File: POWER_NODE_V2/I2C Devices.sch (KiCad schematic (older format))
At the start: 20 parts

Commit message: more WIP
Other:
- moved on the sheet: Q?, R?, U?

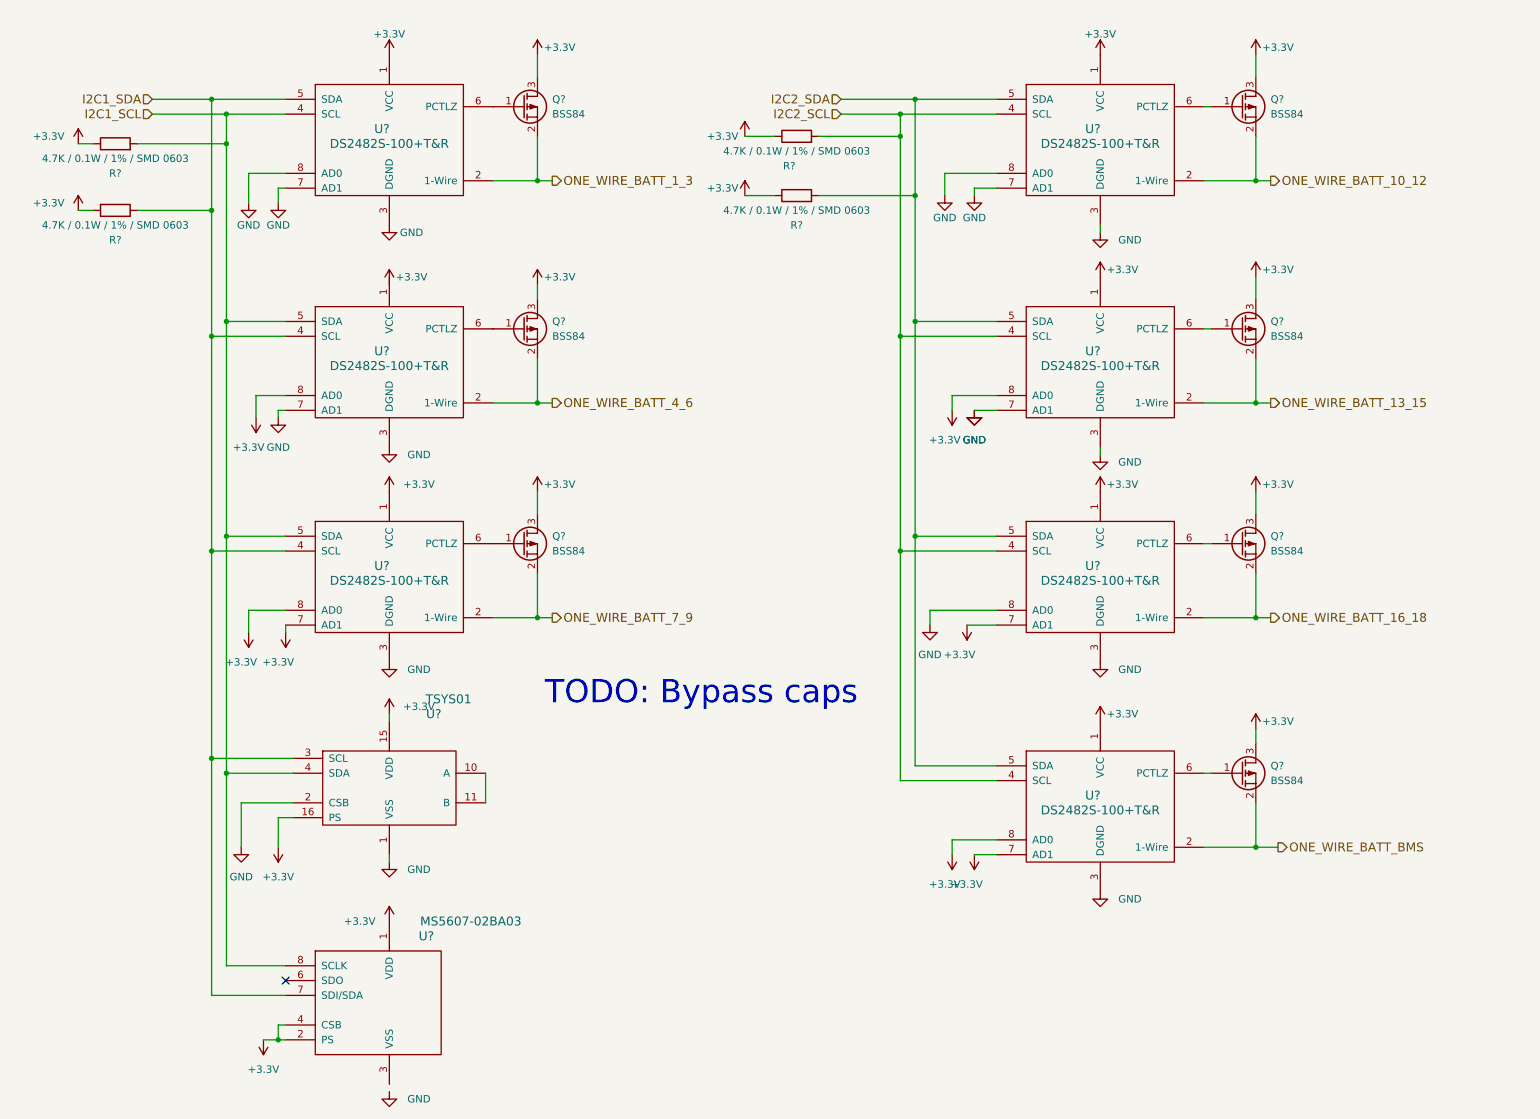
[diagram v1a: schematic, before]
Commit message: Schematic for Power Node V2 mostly done - mostly need connectors
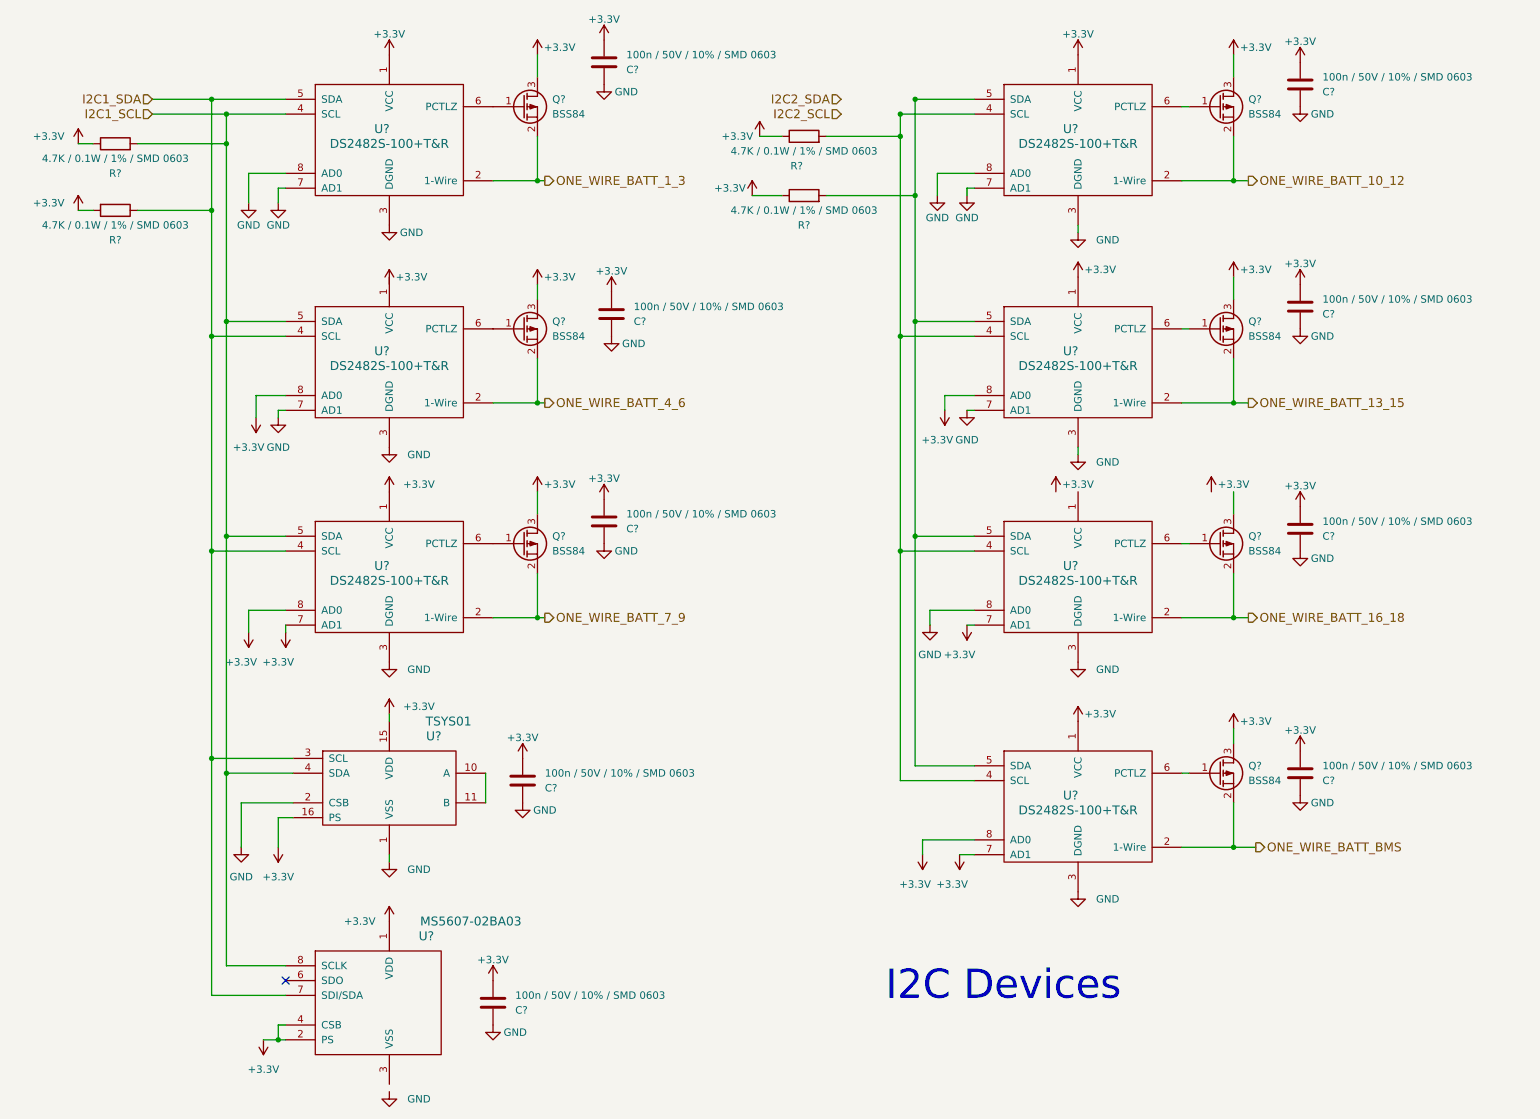
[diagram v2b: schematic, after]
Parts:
- added C? (x9): 100n / 50V / 10% / SMD 0603, symbol C
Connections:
- net +3V3: now also C?.1, C?.1, C?.1, C?.1, C?.1, C?.1, C?.1, C?.1, C?.1; no longer Q?.3 (D), U?.1 (VCC)
- net GND: now also C?.2, C?.2, C?.2, C?.2, C?.2, C?.2, C?.2, C?.2, C?.2
- net I2C2_SCL: no longer R?.2, U?.4 (SCL), U?.4 (SCL), U?.4 (SCL), U?.4 (SCL)
- net I2C2_SDA: no longer R?.2, U?.5 (SDA), U?.5 (SDA), U?.5 (SDA), U?.5 (SDA)
- new net: R?.2, U?.4 (SCL), U?.4 (SCL), U?.4 (SCL), U?.4 (SCL)
- new net: R?.2, U?.5 (SDA), U?.5 (SDA), U?.5 (SDA), U?.5 (SDA)
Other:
- note added: "I2C Devices"
- note removed: "TODO: Bypass caps"
- moved on the sheet: Q?, R?, U?

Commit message: made a lot of footprints, began PCB layout for power node v2
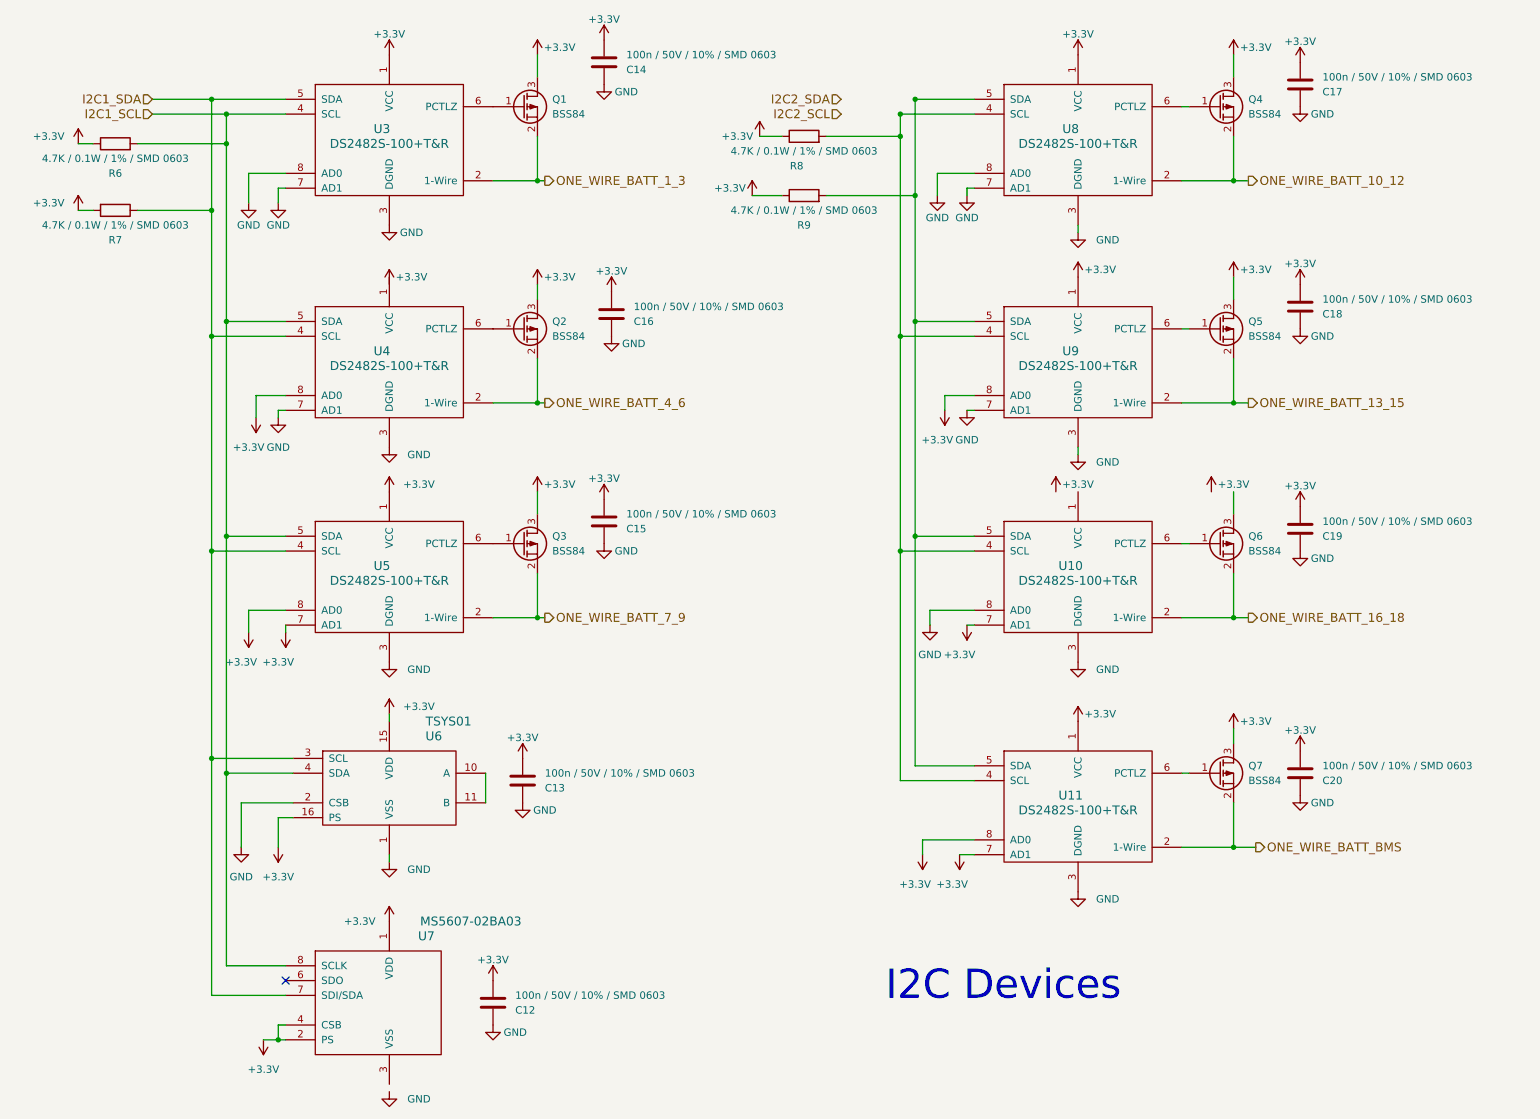
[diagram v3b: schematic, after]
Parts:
- C12, C13, C14, C15, C16, C17, C18, C19, C20: renamed from C?; footprint (none) -> Capacitors_SMD:C_0603
- Q1, Q2, Q3, Q4, Q5, Q6, Q7: renamed from Q?; footprint (none) -> TO_SOT_Packages_SMD:SOT-23
- R6, R7, R8, R9: renamed from R?; footprint (none) -> Resistors_SMD:R_0603
- U10, U11, U3, U4, U5, U8, U9: renamed from U?; footprint (none) -> SMD_Packages:SOIC-8-N
- U6: renamed from U?; footprint (none) -> rLoop Footprints:QFN16_4x4
- U7: renamed from U?; footprint (none) -> rLoop Footprints:ms5607-02ba03

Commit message: Power Node v2 WIP
TODO: 3d models, double check everything, update connector P/N on
schematics, align boards and drill holes
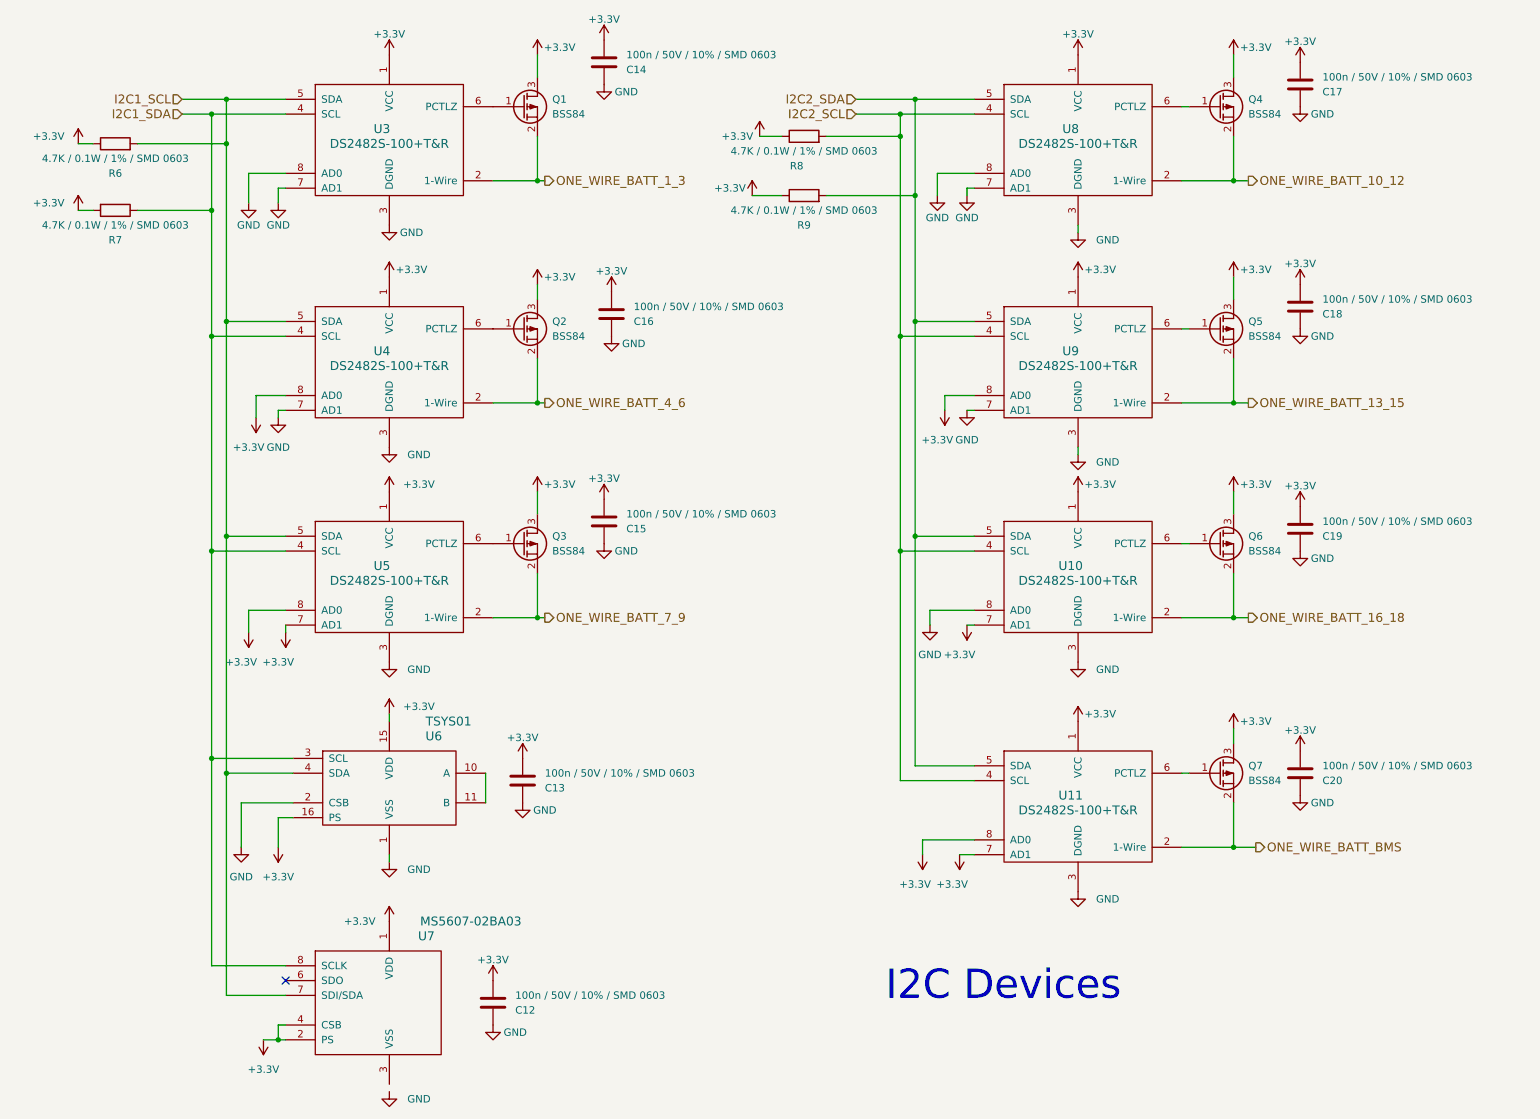
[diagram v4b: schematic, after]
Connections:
- net +3V3: now also Q6.3 (D), U10.1 (VCC), U4.1 (VCC)
- net I2C1_SCL: now also U3.5 (SDA), U7.7 (SDI/SDA); no longer U3.4 (SCL), U7.8 (SCLK)
- net I2C1_SDA: now also U3.4 (SCL), U7.8 (SCLK); no longer U3.5 (SDA), U7.7 (SDI/SDA)
- net I2C2_SCL: now also R8.2, U10.4 (SCL), U11.4 (SCL), U8.4 (SCL), U9.4 (SCL)
- net I2C2_SDA: now also R9.2, U10.5 (SDA), U11.5 (SDA), U8.5 (SDA), U9.5 (SDA)
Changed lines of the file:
@@
 Comment4 ""
 $EndDescr
-Text HLabel 1450 1200 0    60   Input ~ 0
+Text HLabel 1650 1100 0    60   Input ~ 0
 I2C1_SCL
-Text HLabel 1450 1100 0    60   Input ~ 0
+Text HLabel 1650 1200 0    60   Input ~ 0
 I2C1_SDA
-Text HLabel 6100 1200 0    60   Input ~ 0
+Text HLabel 6200 1200 0    60   Input ~ 0
 I2C2_SCL
-Text HLabel 6100 1100 0    60   Input ~ 0
+Text HLabel 6200 1100 0    60   Input ~ 0
 I2C2_SDA
 $Comp
@@
 L +3.3V #PWR034
 U 1 1 594C27E9
-P 3050 2350
-F 0 "#PWR034" H 3050 2200 50  0001 C CNN
-F 1 "+3.3V" H 3200 2400 50  0000 C CNN
-F 2 "" H 3050 2350 50  0001 C CNN
-F 3 "" H 3050 2350 50  0001 C CNN
-	1    3050 2350
+P 3050 2300
+F 0 "#PWR034" H 3050 2150 50  0001 C CNN
+F 1 "+3.3V" H 3200 2350 50  0000 C CNN
+F 2 "" H 3050 2300 50  0001 C CNN
+F 3 "" H 3050 2300 50  0001 C CNN
+	1    3050 2300
 	1    0    0    -1
 $EndComp
@@
 L +3.3V #PWR037
 U 1 1 594C2884
-P 7550 3750
-F 0 "#PWR037" H 7550 3600 50  0001 C CNN
-F 1 "+3.3V" H 7700 3800 50  0000 C CNN
-F 2 "" H 7550 3750 50  0001 C CNN
-F 3 "" H 7550 3750 50  0001 C CNN
-	1    7550 3750
+P 7700 3750
+F 0 "#PWR037" H 7700 3600 50  0001 C CNN
+F 1 "+3.3V" H 7850 3800 50  0000 C CNN
+F 2 "" H 7700 3750 50  0001 C CNN
+F 3 "" H 7700 3750 50  0001 C CNN
+	1    7700 3750
 	1    0    0    -1
 $EndComp
@@
 $EndComp
 Wire Wire Line
-	1450 1100 2350 1100
-Wire Wire Line
-	1450 1200 2350 1200
-Wire Wire Line
 	1950 2600 2350 2600
-Connection ~ 1950 1200
 Wire Wire Line
 	1850 2700 2350 2700
-Connection ~ 1850 1100
 Wire Wire Line
 	1950 4050 2350 4050
@@
 L +3.3V #PWR064
 U 1 1 594C4DD4
-P 8600 3750
-F 0 "#PWR064" H 8600 3600 50  0001 C CNN
-F 1 "+3.3V" H 8750 3800 50  0000 C CNN
-F 2 "" H 8600 3750 50  0001 C CNN
-F 3 "" H 8600 3750 50  0001 C CNN
-	1    8600 3750
+P 8750 3750
+F 0 "#PWR064" H 8750 3600 50  0001 C CNN
+F 1 "+3.3V" H 8900 3800 50  0000 C CNN
+F 2 "" H 8750 3750 50  0001 C CNN
+F 3 "" H 8750 3750 50  0001 C CNN
+	1    8750 3750
 	1    0    0    -1
 $EndComp
@@
 	1    0    0    -1
 $EndComp
-Wire Wire Line
-	1950 6950 2350 6950
 Connection ~ 1950 5650
-Wire Wire Line
-	1850 7150 2350 7150
 Connection ~ 1850 5550
 NoConn ~ 2350 7050
@@
 Connection ~ 2300 7450
 Wire Wire Line
-	1850 1100 1850 7150
-Wire Wire Line
 	5550 1350 5700 1350
 Wire Wire Line
 	5700 1750 5500 1750
-Wire Wire Line
-	1950 1200 1950 6950
 $Comp
 L C C14
@@
 	6750 1600 7000 1600
 Wire Wire Line
-	6600 1100 7000 1100
-Wire Wire Line
-	7000 1200 6500 1200
-Wire Wire Line
 	7000 2600 6600 2600
 Wire Wire Line
@@
 Text Notes 6400 7200 0    197  ~ 0
 I2C Devices
+Wire Wire Line
+	1950 1100 1950 7150
+Connection ~ 1950 1100
+Wire Wire Line
+	1950 7150 2350 7150
+Wire Wire Line
+	1850 6950 2350 6950
+Wire Wire Line
+	1850 1200 1850 6950
+Connection ~ 1850 1200
+Wire Wire Line
+	1650 1100 2350 1100
+Wire Wire Line
+	2350 1200 1650 1200
+Wire Wire Line
+	6200 1100 7000 1100
+Wire Wire Line
+	6200 1200 7000 1200
 $EndSCHEMATC

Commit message: Lot's of progress
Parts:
- U6: footprint rLoop Footprints:QFN16_4x4 -> rLoop_Footprints:QFN16_4x4
- U7: footprint rLoop Footprints:ms5607-02ba03 -> rLoop_Footprints:ms5607-02ba03
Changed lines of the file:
@@
 F 0 "U6" H 3350 6100 60  0000 C CNN
 F 1 "TSYS01" H 3450 6200 60  0000 C CNN
-F 2 "rLoop Footprints:QFN16_4x4" H 3050 5750 60  0001 C CNN
+F 2 "rLoop_Footprints:QFN16_4x4" H 3050 5750 60  0001 C CNN
 F 3 "" H 3050 5750 60  0001 C CNN
 	1    3050 5750
@@
 F 0 "U7" H 3300 7650 60  0000 C CNN
 F 1 "MS5607-02BA03" H 3600 7750 60  0000 C CNN
-F 2 "rLoop Footprints:ms5607-02ba03" H 3050 7200 60  0001 C CNN
+F 2 "rLoop_Footprints:ms5607-02ba03" H 3050 7200 60  0001 C CNN
 F 3 "" H 3050 7200 60  0001 C CNN
 	1    3050 7200
